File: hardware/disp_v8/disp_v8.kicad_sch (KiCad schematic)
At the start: 119 parts, among them J1 Conn_02x16_Odd_Even_FLIP, J2 Conn_01x01_Pin, J3 Conn_01x01_Pin, Q1 2N7002, Q10 2N7002, Q11 2N7002, Q12 2N7002, Q13 2N7002, Q2 2N7002, Q3 2N7002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

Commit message: clean up display v8
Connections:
- net NCOL1: no longer J1.29 (Pin_29)
- net NROW1: no longer J1.28 (Pin_28)
- net NROW2: no longer J1.27 (Pin_27)
- net LA renamed L4
- net LB renamed L1
- net LC renamed L5
- net LD renamed L2
- net LE renamed L6
- net LEDA renamed LED4
- net LED4: now also J1.30 (Pin_30)
- net LEDB renamed LED1
- net LED1: now also J1.27 (Pin_27)
- net LEDC renamed LED5
- net LED5: now also J1.31 (Pin_31)
- net LEDD renamed LED2
- net LED2: now also J1.28 (Pin_28)
- net LEDE renamed LED6
- net LED6: now also J1.32 (Pin_32)
- net LEDF renamed LED3
- net LED3: now also J1.29 (Pin_29)
- net LEDG renamed LED7
- net LEDH renamed LED8
- net LEDI renamed LED9
- net LED9: no longer J1.32 (Pin_32)
- net LEDJ renamed LED10
- net LED10: no longer J1.31 (Pin_31)
- net LEDM1 renamed LEDMG
- net LEDM2 renamed LEDMR
- net LEDMR: no longer J1.30 (Pin_30)
- net LEDM3 renamed LEDMY
- net LF renamed L3
- net LG renamed L7
- net LH renamed L8
- net LI renamed L9
- net LJ renamed L10
- net R0 renamed C1
- net R1 renamed C5
- net R2 renamed C6
- net R3 renamed C7
- net R4 renamed C8
- net R5 renamed C9
- net R6 renamed C4
- net R7 renamed C3
- net R8 renamed C2
- net R9 renamed C10

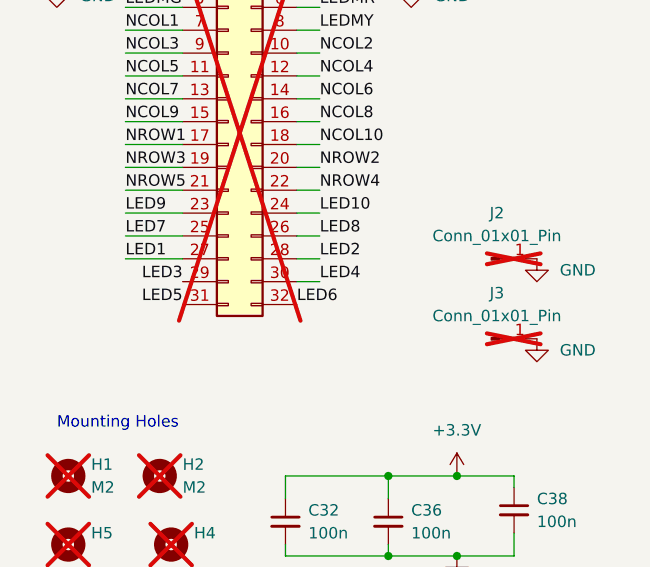
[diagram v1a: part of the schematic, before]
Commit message: relabel row/col/led
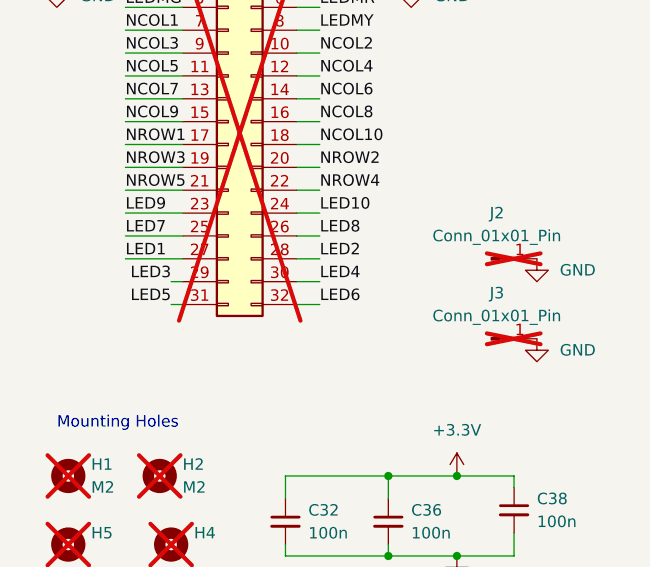
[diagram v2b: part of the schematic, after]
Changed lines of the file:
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@@
+    (stroke (width 0) (type default))
+  )
+  (wire (pts (xy 48.26 62.23) (xy 45.72 62.23))
     (stroke (width 0) (type default))
   )
@@
     (stroke (width 0) (type default))
   )
+  (wire (pts (xy 31.75 62.23) (xy 33.02 62.23))
+    (stroke (width 0) (type default))
+  )
   (wire (pts (xy 44.45 83.82) (xy 44.45 81.28))
     (stroke (width 0) (type default))
@@
   )
   (wire (pts (xy 224.79 147.32) (xy 219.71 147.32))
+    (stroke (width 0) (type default))
+  )
+  (wire (pts (xy 31.75 59.69) (xy 33.02 59.69))
     (stroke (width 0) (type default))
   )
@@
     (effects (font (size 1.27 1.27)) (justify left bottom))
   )
-  (label "LED5" (at 33.02 62.23 180) (fields_autoplaced)
+  (label "LED5" (at 31.75 62.23 180) (fields_autoplaced)
     (effects (font (size 1.27 1.27)) (justify right bottom))
   )
@@
     (effects (font (size 1.27 1.27)) (justify left bottom))
   )
-  (label "LED6" (at 45.72 62.23 0) (fields_autoplaced)
+  (label "LED6" (at 48.26 62.23 0) (fields_autoplaced)
     (effects (font (size 1.27 1.27)) (justify left bottom))
   )
@@
     (effects (font (size 1.27 1.27)) (justify left bottom))
   )
-  (label "LED3" (at 33.02 59.69 180) (fields_autoplaced)
+  (label "LED3" (at 31.75 59.69 180) (fields_autoplaced)
     (effects (font (size 1.27 1.27)) (justify right bottom))
   )

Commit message: order v8 of blink and disp
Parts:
- removed H1, H2, H4, H5: M2, MountingHole:MountingHole_2.2mm_M2, symbol Mechanical:MountingHole
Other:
- note removed: "Mounting Holes"
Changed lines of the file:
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@@
   (title_block
     (title "Disp")
-    (date "2023-11-10")
+    (date "2023-11-12")
     (rev "V8")
     (company "Cullen Jennings")
@@
     (stroke (width 0) (type default))
   )
-  (text "Mounting Holes" (at 19.05 76.2 0)
-    (effects (font (size 1.27 1.27)) (justify left bottom))
-  )
   (label "LED3" (at 73.66 140.97 0) (fields_autoplaced)
     (effects (font (size 1.27 1.27)) (justify left bottom))
@@
     )
   )
-  (symbol (lib_id "Mechanical:MountingHole") (at 30.48 81.28 0) (unit 1)
-    (in_bom no) (on_board yes) (dnp yes) (fields_autoplaced)
-    (property "Reference" "H2" (at 33.02 80.01 0)
-      (effects (font (size 1.27 1.27)) (justify left))
-    )
-    (property "Value" "M2" (at 33.02 82.55 0)
-      (effects (font (size 1.27 1.27)) (justify left))
-    )
-    (property "Footprint" "MountingHole:MountingHole_2.2mm_M2" (at 30.48 81.28 0)
-      (effects (font (size 1.27 1.27)) hide)
-    )
-    (property "Datasheet" "~" (at 30.48 81.28 0)
-      (effects (font (size 1.27 1.27)) hide)
-    )
-    (instances
-      (project "disp_v8"
-        (path "/bd4d3b9a-07c1-4a53-9c94-2893f3e869d4"
-          (reference "H2") (unit 1)
-        )
-      )
-    )
-  )
   (symbol (lib_id "Device:R_US") (at 62.23 132.08 0) (unit 1)
     (in_bom yes) (on_board yes) (dnp no) (fields_autoplaced)
@@
     )
   )
-  (symbol (lib_id "Mechanical:MountingHole") (at 31.75 88.9 0) (unit 1)
-    (in_bom no) (on_board yes) (dnp yes)
-    (property "Reference" "H4" (at 34.29 87.63 0)
-      (effects (font (size 1.27 1.27)) (justify left))
-    )
-    (property "Value" "M2" (at 30.48 92.71 0)
-      (effects (font (size 1.27 1.27)) (justify left))
-    )
-    (property "Footprint" "MountingHole:MountingHole_2.2mm_M2" (at 31.75 88.9 0)
-      (effects (font (size 1.27 1.27)) hide)
-    )
-    (property "Datasheet" "~" (at 31.75 88.9 0)
-      (effects (font (size 1.27 1.27)) hide)
-    )
-    (instances
-      (project "disp_v8"
-        (path "/bd4d3b9a-07c1-4a53-9c94-2893f3e869d4"
-          (reference "H4") (unit 1)
-        )
-      )
-    )
-  )
   (symbol (lib_id "Device:R_US") (at 138.43 193.04 180) (unit 1)
     (in_bom yes) (on_board yes) (dnp no)
@@
     )
   )
-  (symbol (lib_id "Mechanical:MountingHole") (at 20.32 81.28 0) (unit 1)
-    (in_bom no) (on_board yes) (dnp yes) (fields_autoplaced)
-    (property "Reference" "H1" (at 22.86 80.01 0)
-      (effects (font (size 1.27 1.27)) (justify left))
-    )
-    (property "Value" "M2" (at 22.86 82.55 0)
-      (effects (font (size 1.27 1.27)) (justify left))
-    )
-    (property "Footprint" "MountingHole:MountingHole_2.2mm_M2" (at 20.32 81.28 0)
-      (effects (font (size 1.27 1.27)) hide)
-    )
-    (property "Datasheet" "~" (at 20.32 81.28 0)
-      (effects (font (size 1.27 1.27)) hide)
-    )
-    (instances
-      (project "disp_v8"
-        (path "/bd4d3b9a-07c1-4a53-9c94-2893f3e869d4"
-          (reference "H1") (unit 1)
-        )
-      )
-    )
-  )
   (symbol (lib_id "Device:R_US") (at 107.95 193.04 180) (unit 1)
     (in_bom yes) (on_board yes) (dnp no)
@@
         )
       )
-    )
-  )
-  (symbol (lib_id "Mechanical:MountingHole") (at 20.32 88.9 0) (unit 1)
-    (in_bom no) (on_board yes) (dnp yes)
-    (property "Reference" "H5" (at 22.86 87.63 0)
-      (effects (font (size 1.27 1.27)) (justify left))
-    )
-    (property "Value" "M2" (at 19.05 92.71 0)
-      (effects (font (size 1.27 1.27)) (justify left))
-    )
-    (property "Footprint" "MountingHole:MountingHole_2.2mm_M2" (at 20.32 88.9 0)
-      (effects (font (size 1.27 1.27)) hide)
-    )
-    (property "Datasheet" "~" (at 20.32 88.9 0)
-      (effects (font (size 1.27 1.27)) hide)
-    )
-    (instances
-      (project "disp_v8"
-        (path "/bd4d3b9a-07c1-4a53-9c94-2893f3e869d4"
-          (reference "H5") (unit 1)
-        )
-      )

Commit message: update disp schematics for new footprints / symbols
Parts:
- J1: footprint blinky_footprints:PinSocket_2x16_P2.54mm_Vertical_FLIP -> Connector_PinHeader_2.54mm:PinHeader_2x16_P2.54mm_Vertical
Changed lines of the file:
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@@
       (effects (font (size 1.27 1.27)))
     )
-    (property "Footprint" "blinky_footprints:PinSocket_2x16_P2.54mm_Vertical_FLIP" (at 38.1 41.91 0)
+    (property "Footprint" "Connector_PinHeader_2.54mm:PinHeader_2x16_P2.54mm_Vertical" (at 38.1 41.91 0)
       (effects (font (size 1.27 1.27)) hide)
     )
